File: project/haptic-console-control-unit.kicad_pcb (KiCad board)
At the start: 2 copper layers, 88 x 131 mm, 30 parts, among them J1 JST-XH-5, J2 JST-XH-5, U1 Teensy 4.1

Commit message: Add TP1-TP5 test points (SDA/SCL/GND/+3V3/+5V) to schematic and both boards
Schematic: 5 TestPoint symbols wired near the R12/R13 pullup network.
Manufactured board: 5 THT test pads routed around the existing autorouted
copper. Perfboard: real male 2.54mm header pins (not flat pads) at the
board's last column, with S1-S6 shifted one column left to clear them.
Wiring guide and README updated to match; full session notes in CLAUDE.md.

Co-Authored-By: Claude Sonnet 5 <noreply@anthropic.com>
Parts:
- added TP1: TP_SDA, TestPoint_THTPad_D1.5mm_Drill0.7mm, F.Cu at (30.0, 58.5)
- added TP2: TP_3V3, TestPoint_THTPad_D1.5mm_Drill0.7mm, F.Cu at (38.0, 58.5)
- added TP3: TP_GND, TestPoint_THTPad_D1.5mm_Drill0.7mm, F.Cu at (50.0, 61.0)
- added TP4: TP_5V, TestPoint_THTPad_D1.5mm_Drill0.7mm, F.Cu at (47.5, 42.5)
- added TP5: TP_SCL, TestPoint_THTPad_D1.5mm_Drill0.7mm, F.Cu at (50.2, 53.0)
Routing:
- net /SDA: track 128.8 -> 135.5 mm
- net +5V: track 118.1 -> 123.1 mm
- net +3V3: track 172.8 -> 177.5 mm
- net GND: track 408.6 -> 413.1 mm
- net /SCL: track 121.9 -> 125.1 mm

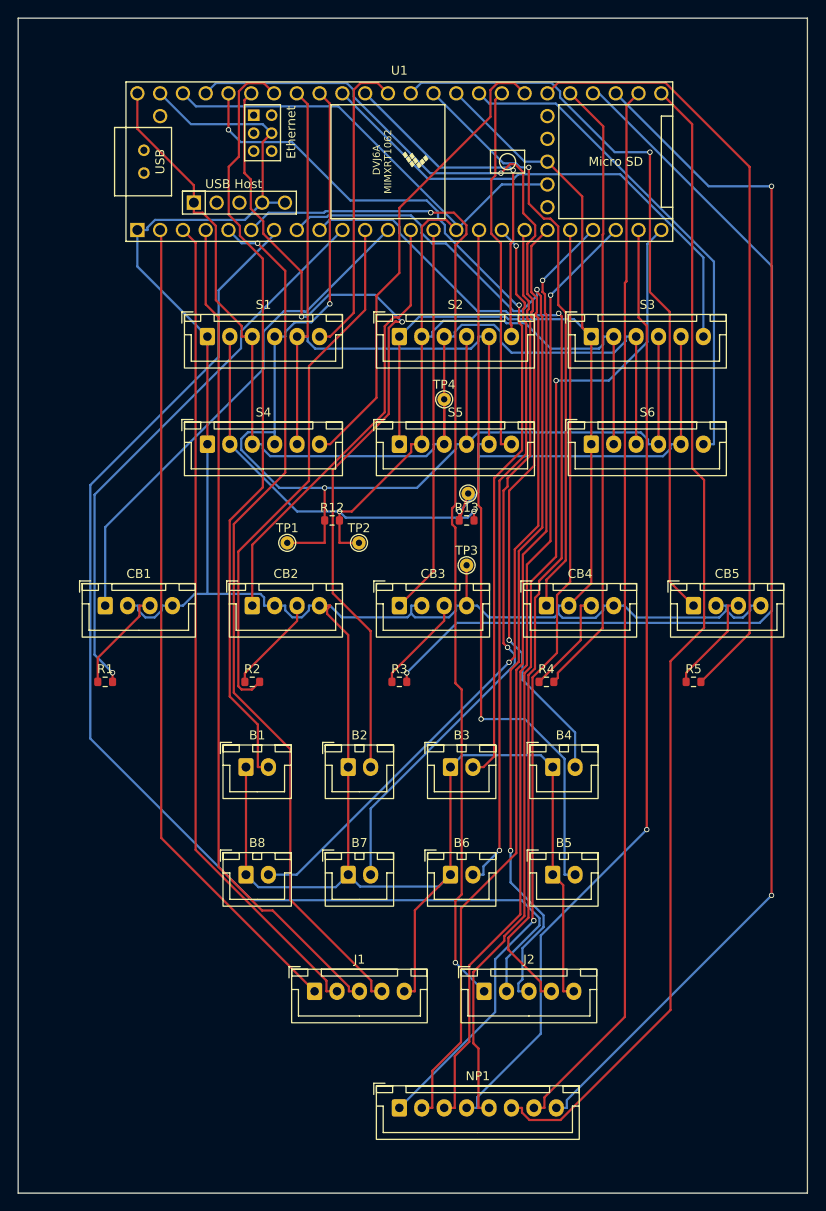
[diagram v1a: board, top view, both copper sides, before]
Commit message: Remap every GPIO to its nearest Teensy pin, fix stale CB4/D13 doc note
Every connector signal (B1-B8, CB1-5, J1/J2, NP1, LED1-5) now sits on
whichever Teensy pin is physically closest to it on the board instead
of a contiguous functional block, solved as a bipartite matching over
Manhattan wire distance. Schematic labels, the manufactured board's
nets/routing, and the perfboard's hand-wiring layout were all
regenerated from the new scripts/pin_map.json; docs and renders follow.

Also drops the panel wiring guide's leftover "CB4 sits on pin 13"
hazard callout, which the remap made false (D13 moved to NP1's row-0
output) - the equivalent warning already lives in the NP1 section.

Co-Authored-By: Claude Sonnet 5 <noreply@anthropic.com>
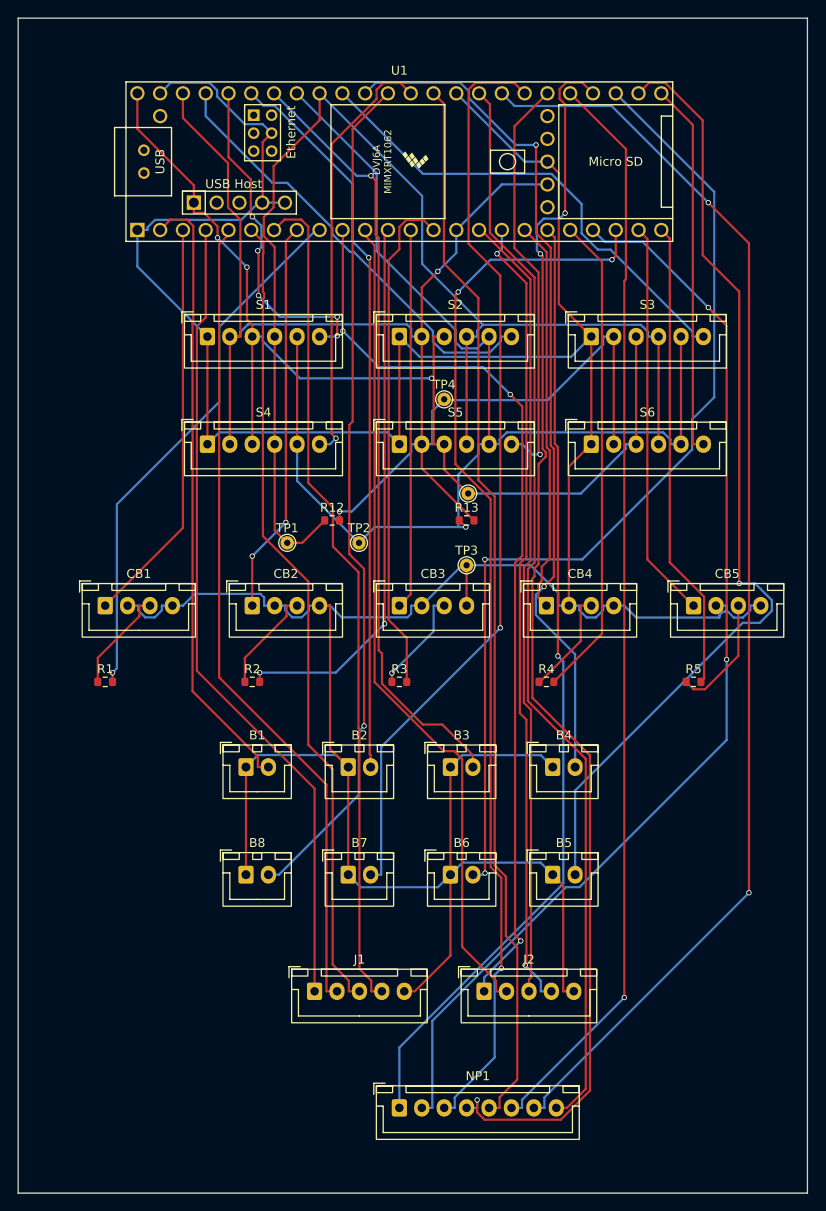
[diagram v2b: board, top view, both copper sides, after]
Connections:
- B1 pad 2: /D20 -> /D0
- B3 pad 2: /D22 -> /D20
- B4 pad 2: /D23 -> /D16
- B5 pad 2: /D24 -> /D34
- B6 pad 2: /D25 -> /D35
- B7 pad 2: /D26 -> /D39
- B8 pad 2: /D27 -> /D15
- CB1 pad 1: /D10 -> /D1
- CB2 pad 1: /D11 -> /D6
- CB3 pad 1: /D12 -> /D11
- CB4 pad 1: /D13 -> /D26
- CB5 pad 1: /D14 -> /D31
- J1 pad 1: /D0 -> /D2
- J1 pad 2: /D1 -> /D3
- J1 pad 3: /D2 -> /D4
- J1 pad 4: /D3 -> /D5
- J2 pad 1: /D4 -> /D8
- J2 pad 2: /D5 -> /D9
- J2 pad 3: /D6 -> /D24
- J2 pad 4: /D7 -> /D25
- NP1 pad 1: /D28 -> /D27
- NP1 pad 4: /D31 -> /D36
- NP1 pad 5: /D32 -> /D13
- NP1 pad 6: /D33 -> /D37
- NP1 pad 7: /D34 -> /D40
- NP1 pad 8: /D35 -> /D41
- R1 pad 2: /D8 -> /D7
- R2 pad 2: /D9 -> /D10
- R3 pad 2: /D36 -> /D12
- R4 pad 2: /D37 -> /D28
- R5 pad 2: /D38 -> /D32
- S1 pad 3: +5V -> /+5V
- S2 pad 3: +5V -> /+5V
- S3 pad 3: +5V -> /+5V
- S4 pad 3: +5V -> /+5V
- S5 pad 3: +5V -> /+5V
- S6 pad 3: +5V -> /+5V
- TP2 pad 1: +3V3 -> /SCL
- TP4 pad 1: +5V -> +3V3
- TP5 pad 1: /SCL -> /+5V
- U1 pad 25: /D33 -> /IRQ6
- U1 pad 30: /D38 -> /IRQ5
- U1 pad 31: /IRQ4 -> /D39
- U1 pad 32: /IRQ5 -> /D40
- U1 pad 33: /IRQ6 -> /D41
- U1 pad 36: /D14 -> /IRQ4
- U1 pad 37: /IRQ1 -> /D15
- U1 pad 38: /IRQ2 -> /D16
- U1 pad 44: /D22 -> /IRQ1
- U1 pad 45: /D23 -> /IRQ2
- U1 pad 48: +5V -> /+5V
- U1 pad 55: +5V -> /+5V
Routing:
- net /D40: track 0.00 -> 141.5 mm, vias 0 -> 2
- net /D33: track 129.4 -> 0.00 mm
- net +5V: track 123.1 -> 0.00 mm
- net /+5V: track 0.00 -> 121.8 mm, vias 0 -> 3
- net /D41: track 0.00 -> 120.7 mm
- net /D23: track 113.2 -> 0.00 mm, vias 2 -> 0
- net /D39: track 0.00 -> 102.7 mm, vias 0 -> 1
- net /D22: track 100.1 -> 0.00 mm, vias 2 -> 0
- net /D16: track 0.00 -> 95.7 mm, vias 0 -> 2
- net /D15: track 0.00 -> 94.7 mm, vias 0 -> 1
- net /D38: track 86.6 -> 0.00 mm
- net /D14: track 83.3 -> 0.00 mm, vias 1 -> 0
- net /D6: track 117.7 -> 43.9 mm
- net /D31: track 107.3 -> 44.4 mm, vias 1 -> 0
- net /D32: track 111.4 -> 52.5 mm, vias 1 -> 0
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
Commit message: Resync every KiCad artifact to the current pin map (LED4 frozen on D13)
R4's LED jumper was re-landed from R29 (D16 = J1 pin 4, already soldered) to
O29 (D13), clearing the hardware conflict flagged last session. LED4 joins the
frozen set, which now holds 18 already-soldered conductors: B1-B8, J1/J2, LED4,
LED5. Freezing it costs nothing -- the solver had already chosen D13 -- so the
map stays at 1356.3 mm total Manhattan run, 61.0 mm longest wire.

- Schematic: 44 net labels renamed to their GPIO names (D<n>) via delete +
  re-add at identical coordinates. 2244 lines, 141 labels, ERC 0/0, 63 nets,
  all 40 signals verified on their intended U1 pin from the netlist libparts.
- Manufactured board: re-netted from a fresh netlist dump and re-routed via
  DSN -> Freerouting -> SES. 654 segments, 35 vias, DRC 0 violations /
  0 unconnected pads. Needed -mp 40; -mp 6 exited clean at 991.13 with one
  net still unrouted.
- Perfboard: R1-R5 moved upright beside their own CB in KiCad (they had only
  been patched into board_model.json before), 223 back-side jumper legs across
  6 tiers, 0 emit violations, 0 same-tier conflicts. Pristine DRC baseline is
  now 451 (was 478) -- moving the resistors off row 48 removed 27 violations --
  and the wired board's violation multiset is identical to it.
- Gerbers re-exported and re-zipped; all six renders regenerated, with zero
  wire overflow in all six colours confirmed by pixel measurement.
- Docs: wiring-guide.html regenerated (107 connections, 3006 mm, 157 pads /
  223 wires), panel-wiring-guide.html and README.md updated to match.

Co-Authored-By: Claude Opus 5 <noreply@anthropic.com>
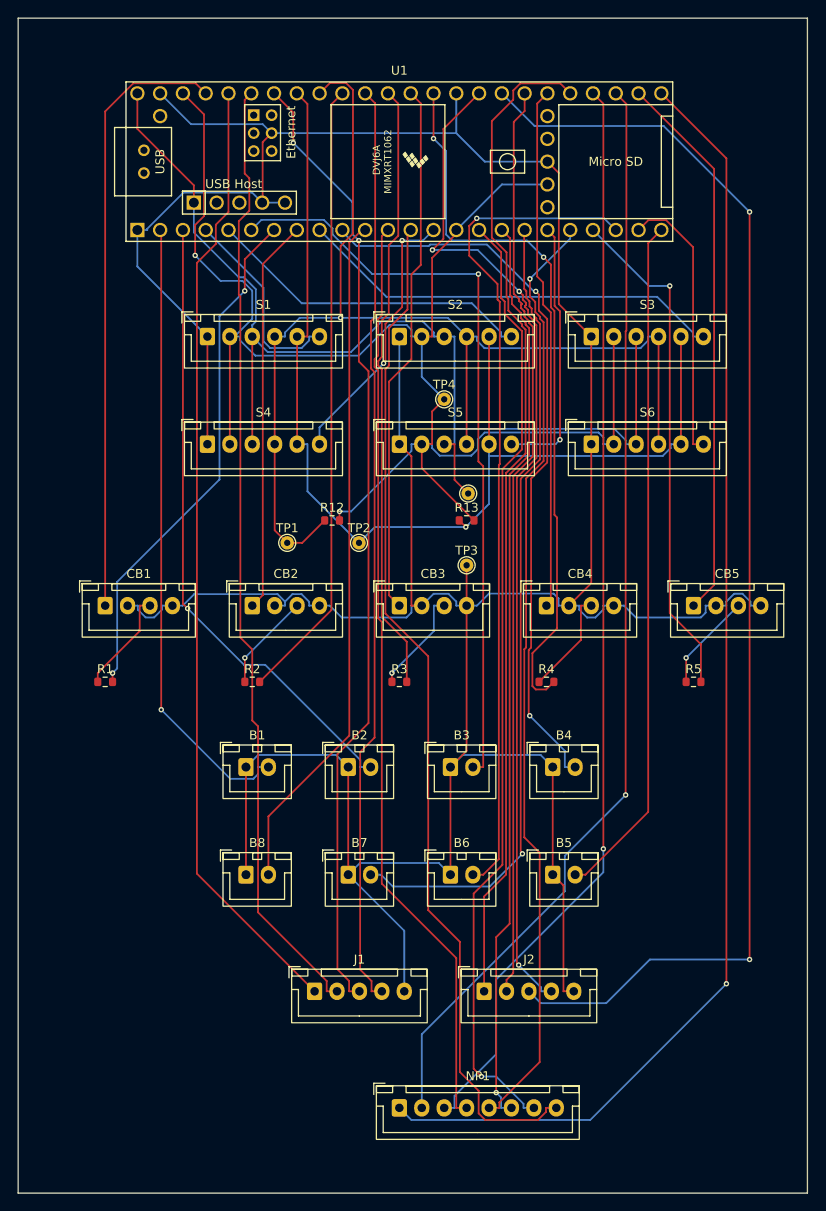
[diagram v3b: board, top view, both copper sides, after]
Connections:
- B2 pad 2: /D21 -> /D1
- B3 pad 2: /D20 -> /D4
- B4 pad 2: /D16 -> /D8
- B5 pad 2: /D34 -> /D32
- B6 pad 2: /D35 -> /D30
- B7 pad 2: /D39 -> /D26
- B8 pad 2: /D15 -> /D9
- CB1 pad 1: /D1 -> /D23
- CB3 pad 1: /D11 -> /D14
- CB4 pad 1: /D26 -> /D38
- CB5 pad 1: /D31 -> /D34
- J1 pad 1: /D2 -> /D22
- J1 pad 2: /D3 -> /D21
- J1 pad 3: /D4 -> /D20
- J1 pad 4: /D5 -> /D16
- J2 pad 1: /D8 -> /D37
- J2 pad 2: /D9 -> /D39
- J2 pad 3: /D24 -> /D40
- J2 pad 4: /D25 -> /D41
- NP1 pad 1: /D27 -> /D33
- NP1 pad 2: /D29 -> /D35
- NP1 pad 3: /D30 -> /D36
- NP1 pad 4: /D36 -> /D10
- NP1 pad 5: /D13 -> /D28
- NP1 pad 6: /D37 -> /D25
- NP1 pad 7: /D40 -> /D24
- NP1 pad 8: /D41 -> /D11
- R1 pad 2: /D7 -> /D5
- R2 pad 2: /D10 -> /D17
- R3 pad 2: /D12 -> /D15
- R4 pad 2: /D28 -> /D13
- R5 pad 2: /D32 -> /D29
- S1 pad 6: /IRQ1 -> /D2
- S2 pad 6: /IRQ2 -> /D3
- S3 pad 6: /IRQ3 -> /D7
- S4 pad 6: /IRQ4 -> /D12
- S5 pad 6: /IRQ5 -> /D27
- S6 pad 6: /IRQ6 -> /D31
- U1 pad 25: /IRQ6 -> /D33
- U1 pad 30: /IRQ5 -> /D38
- U1 pad 36: /IRQ4 -> /D14
- U1 pad 39: /IRQ3 -> /D17
- U1 pad 44: /IRQ1 -> /D22
- U1 pad 45: /IRQ2 -> /D23
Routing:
- net /D33: track 0.00 -> 145.6 mm, vias 0 -> 1
- net /D22: track 0.00 -> 107.0 mm
- net /D27: track 106.2 -> 29.6 mm
- net /D11: track 42.4 -> 113.7 mm
- net /D17: track 0.00 -> 69.4 mm
- net /D2: track 90.7 -> 22.4 mm
- net /D23: track 0.00 -> 68.1 mm
- net /D29: track 122.2 -> 56.7 mm, vias 2 -> 1
- net /D14: track 0.00 -> 59.5 mm
- net /D38: track 0.00 -> 58.4 mm
- net /D3: track 91.4 -> 36.7 mm
- net /IRQ3: track 53.7 -> 0.00 mm
- net /D28: track 54.1 -> 105.0 mm, vias 0 -> 1
- net /IRQ2: track 49.7 -> 0.00 mm
- net /IRQ4: track 47.8 -> 0.00 mm, vias 1 -> 0
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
